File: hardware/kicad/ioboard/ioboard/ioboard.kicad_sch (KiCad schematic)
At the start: 0 parts

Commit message: power: schematic capture complete (protection chain, 4 rails, isolated analog, hierarchical/global labels)
Commits the finished power.kicad_sch: J1/F1/Q1/U1/U2 protection chain,
four regulated DC-DC modules (U3-U6) with correct feedback networks,
TVS3300 surge clamp, R1SX-3.33.3-R isolated analog supply. GND_LOGIC
exposed as a global label; the four rail outputs + GND_ANALOG_ISO
exposed as hierarchical sheet pins on the parent ioboard.kicad_sch.
ERC clean apart from expected 'not connected to anything' warnings on
labels with no consumer yet (no other subsystem sheet exists).

Also fixes .gitignore: '#auto_saved_files#' was being silently treated
as a comment line (leading '#'), not a pattern -- never actually
excluded anything. Escaped it so it works.

Co-Authored-By: Claude Sonnet 5 <noreply@anthropic.com>
Claude-Session: https://claude.ai/code/session_011Mk4ACKLUzGL8p2SUjrweQ
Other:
- added sheet power (power.kicad_sch)
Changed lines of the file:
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@@
 	(generator_version "9.0")
 	(paper "A4")
+	(sheet
+		(at 31.75 33.02)
+		(size 33.02 38.1)
+		(exclude_from_sim no)
+		(in_bom yes)
+		(on_board yes)
+		(dnp no)
+		(fields_autoplaced yes)
+		(stroke
+			(width 0.1524)
+			(type solid)
+		)
+		(fill
+			(color 0 0 0 0.0000)
+		)
+		(property "Sheetname" "power"
+			(at 31.75 31.4434 0)
+			(effects
+				(font
+					(size 3 3)
+				)
+				(justify left bottom)
+			)
+		)
+		(property "Sheetfile" "power.kicad_sch"
+			(at 31.75 71.9966 0)
+			(effects
+				(font
+					(size 2 2)
+				)
+				(justify left top)
+			)
+		)
+		(instances
+			(project "ioboard"
+				(path "/a0fa9f92-ef51-408b-9617-1545f9e9dad8"
+					(page "2")
+				)
+			)
+		)
+	)
 	(sheet_instances
 		(path "/"

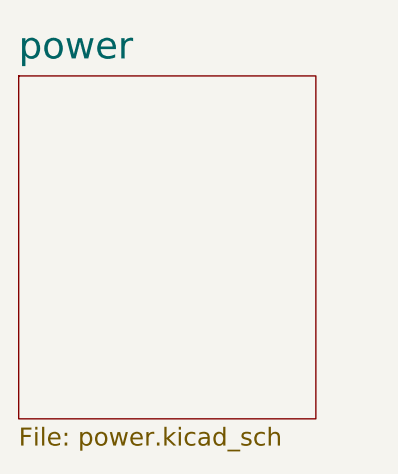
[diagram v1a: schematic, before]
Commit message: power: further schematic refinements (C1 value, EN wiring, and other fixes)
Continued hand-editing in KiCad after the last commit -- captures the
current state of power.kicad_sch and ioboard.kicad_sch.

Co-Authored-By: Claude Sonnet 5 <noreply@anthropic.com>
Claude-Session: https://claude.ai/code/session_011Mk4ACKLUzGL8p2SUjrweQ
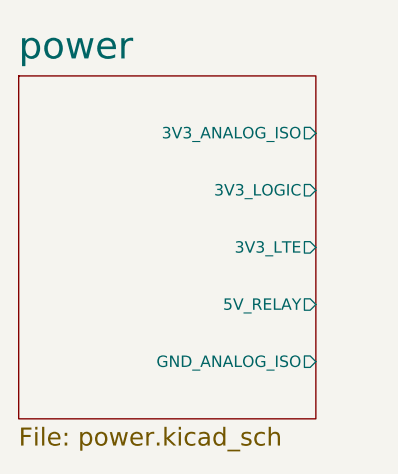
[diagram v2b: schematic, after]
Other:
- sheet power ports: added 3V3_ANALOG_ISO, 3V3_LOGIC, 3V3_LTE, 5V_RELAY, GND_ANALOG_ISO; removed none
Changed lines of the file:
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@@
+			)
+		)
+		(pin "3V3_ANALOG_ISO" output
+			(at 64.77 39.37 0)
+			(effects
+				(font
+					(size 1.27 1.27)
+				)
+				(justify right)
+			)
+		)
+		(pin "3V3_LOGIC" output
+			(at 64.77 45.72 0)
+			(effects
+				(font
+					(size 1.27 1.27)
+				)
+				(justify right)
+			)
+		)
+		(pin "3V3_LTE" output
+			(at 64.77 52.07 0)
+			(effects
+				(font
+					(size 1.27 1.27)
+				)
+				(justify right)
+			)
+		)
+		(pin "5V_RELAY" output
+			(at 64.77 58.42 0)
+			(effects
+				(font
+					(size 1.27 1.27)
+				)
+				(justify right)
+			)
+		)
+		(pin "GND_ANALOG_ISO" output
+			(at 64.77 64.77 0)
+			(effects
+				(font
+					(size 1.27 1.27)
+				)
+				(justify right)
 			)
 		)

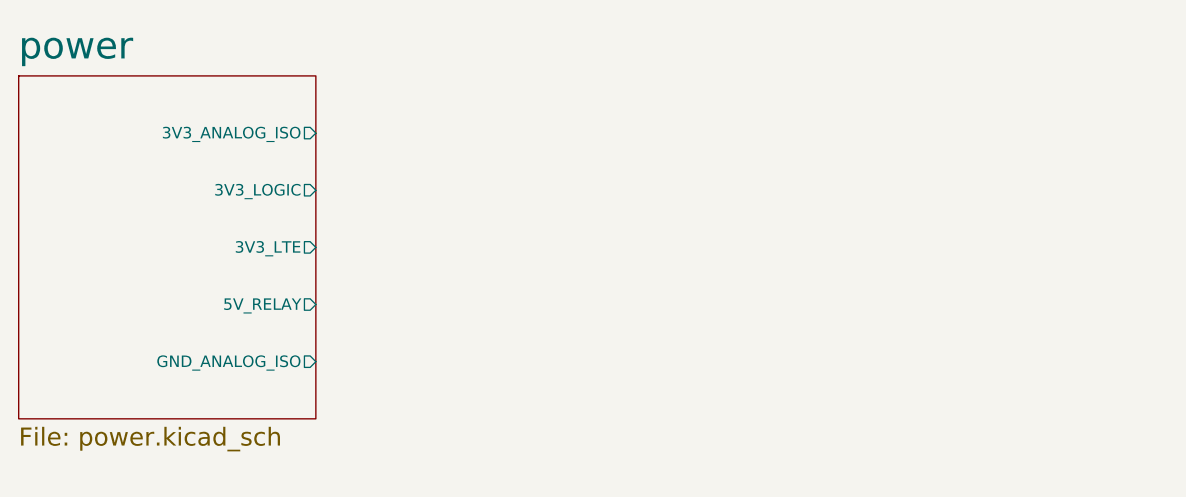
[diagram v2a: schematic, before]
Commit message: digital-inputs: schematic capture complete, plan closed out
All 8 channels wired across two LTV-247 ICs (U7 A-D, U8 A-D), each
identical: field input -> series R (2.4k) -> LED -> reverse-protection
diode (1N4148) -> GND_FIELD_DI, phototransistor -> pull-up (10k) to
3V3_LOGIC + filter cap (100nF) to GND_LOGIC. Field connector J2
(Phoenix Contact MC 1,5/9-ST-3,5, same family as the power input
connector) terminates all 8 channels plus the shared common return.

Also establishes a clearer project-wide label-scoping convention,
worked out this session: local labels for anything that never leaves
one sheet, hierarchical labels + an explicit wire on the parent sheet
for anything shared between a specific set of subsystems (now used for
3V3_LOGIC between power and digital_inputs), global labels reserved
for GND_LOGIC only since it's used near-universally. This replaces the
temporary local-only placeholder for 3V3_LOGIC and wires it properly
through ioboard.kicad_sch's root sheet.

Connector, verification checklist, acceptance criteria, and BOM all
closed out in docs/subsystems/digital-inputs.md; datasheets README
updated with the LTV-247 and connector sources.

Co-Authored-By: Claude Sonnet 5 <noreply@anthropic.com>
Claude-Session: https://claude.ai/code/session_011Mk4ACKLUzGL8p2SUjrweQ
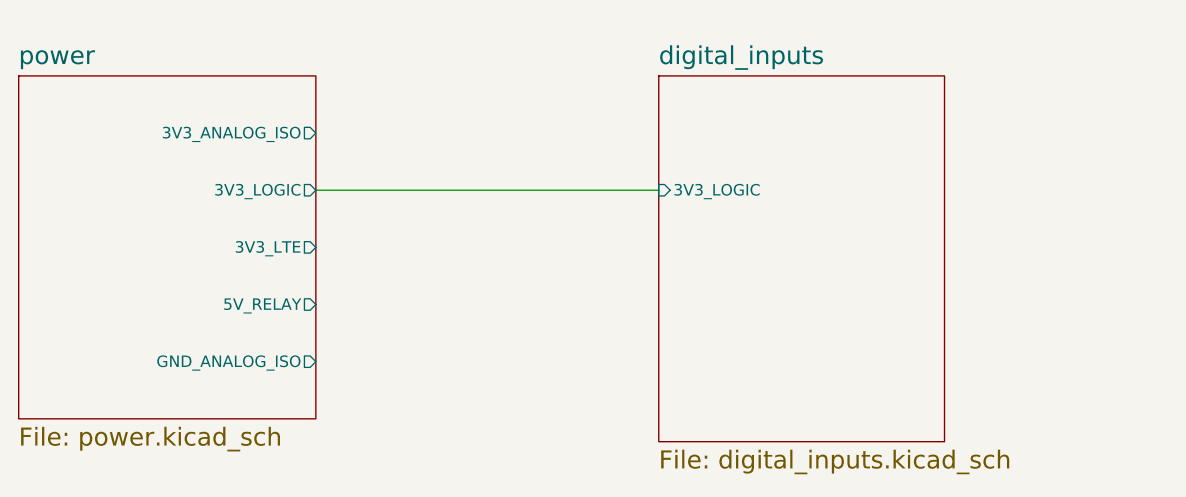
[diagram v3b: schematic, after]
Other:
- added sheet digital_inputs (digital_inputs.kicad_sch)
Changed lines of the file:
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@@
 	(generator_version "9.0")
 	(paper "A4")
+	(wire
+		(pts
+			(xy 64.77 45.72) (xy 102.87 45.72)
+		)
+		(stroke
+			(width 0)
+			(type default)
+		)
+	)
 	(sheet
 		(at 31.75 33.02)
@@
 		)
 		(property "Sheetname" "power"
-			(at 31.75 31.4434 0)
+			(at 31.75 31.9434 0)
 			(effects
 				(font
-					(size 3 3)
+					(size 2 2)
 				)
 				(justify left bottom)
@@
 				)
 			)
+		)
+	)
+	(sheet
+		(at 102.87 33.02)
+		(size 31.75 40.64)
+		(exclude_from_sim no)
+		(in_bom yes)
+		(on_board yes)
+		(dnp no)
+		(fields_autoplaced yes)
+		(stroke
+			(width 0.1524)
+			(type solid)
+		)
+		(fill
+			(color 0 0 0 0.0000)
+		)
+		(property "Sheetname" "digital_inputs"
+			(at 102.87 31.9434 0)
+			(effects
+				(font
+					(size 2 2)
+				)
+				(justify left bottom)
+			)
+		)
+		(property "Sheetfile" "digital_inputs.kicad_sch"
+			(at 102.87 74.5366 0)
+			(effects
+				(font
+					(size 2 2)
+				)
+				(justify left top)
+			)
+		)
+		(pin "3V3_LOGIC" input
+			(at 102.87 45.72 180)
+			(effects
+				(font
+					(size 1.27 1.27)
+				)
+				(justify left)
+			)
+		)
+		(instances
+			(project "ioboard"
+				(path "/a0fa9f92-ef51-408b-9617-1545f9e9dad8"
+					(page "3")
+				)
+			)

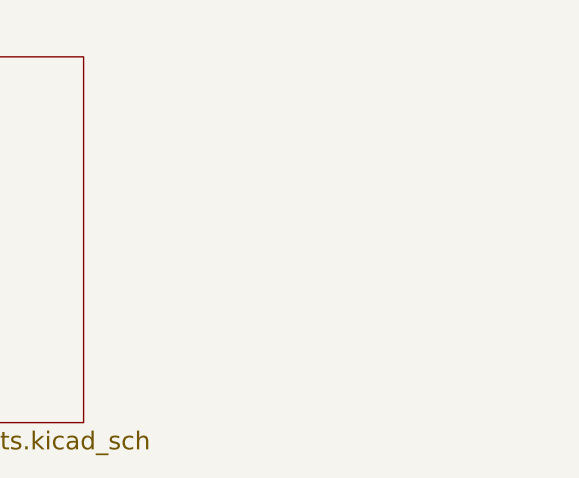
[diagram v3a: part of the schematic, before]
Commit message: relay-outputs: build plan + driver stage and connector locked
Panasonic ALDP105 relay re-verified against Panasonic's own product page
(coil 5V/125ohm/40mA, contacts 5A/277VAC SPST-NO). Driver stage designed
around a generic MMBT3904 NPN transistor (Nexperia datasheet): 510ohm base
resistor sized for ~3.8x saturation margin using the conservative hFE_min,
10k base pull-down for a defined-off boot state, 1N4148 flyback diode
reusing the part already qualified in digital-inputs.

Connector: Phoenix Contact MC 1,5/8-ST-3,5 (1840421), same family as J1/J2,
8 independent positions (COM+NO per channel, no shared common). Flagged in
the plan doc: this connector's 160V rating is below the relay's own 277VAC
contact rating, so the connector -- not the relay -- is the practical
ceiling on what this board switches; documented as an accepted default,
swappable later without touching the schematic if higher voltage is needed.

Also includes the relay_outputs sheet already added to ioboard.kicad_sch
in KiCad (empty template, no components placed yet) and a harmless UUID
regeneration in digital_inputs.kicad_sch from KiCad re-saving the project.

Co-Authored-By: Claude Sonnet 5 <noreply@anthropic.com>
Claude-Session: https://claude.ai/code/session_011Mk4ACKLUzGL8p2SUjrweQ
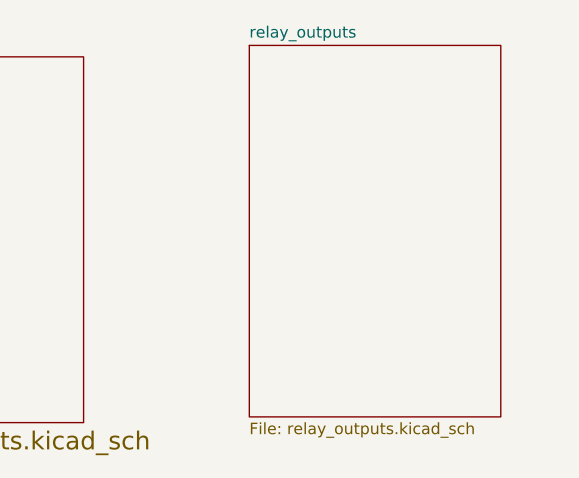
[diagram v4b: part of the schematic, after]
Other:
- added sheet relay_outputs (relay_outputs.kicad_sch)
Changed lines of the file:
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@@
+	)
+	(sheet
+		(at 153.035 31.75)
+		(size 27.94 41.275)
+		(exclude_from_sim no)
+		(in_bom yes)
+		(on_board yes)
+		(dnp no)
+		(fields_autoplaced yes)
+		(stroke
+			(width 0.1524)
+			(type solid)
+		)
+		(fill
+			(color 0 0 0 0.0000)
+		)
+		(property "Sheetname" "relay_outputs"
+			(at 153.035 31.0384 0)
+			(effects
+				(font
+					(size 1.27 1.27)
+				)
+				(justify left bottom)
+			)
+		)
+		(property "Sheetfile" "relay_outputs.kicad_sch"
+			(at 153.035 73.6096 0)
+			(effects
+				(font
+					(size 1.27 1.27)
+				)
+				(justify left top)
+			)
+		)
+		(instances
+			(project "ioboard"
+				(path "/a0fa9f92-ef51-408b-9617-1545f9e9dad8"
+					(page "4")
+				)
+			)
+		)
 	)
 	(sheet
